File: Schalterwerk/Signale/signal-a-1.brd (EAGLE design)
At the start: 86 x 30.5 mm, 29 parts, among them Q1 NPN-23, Q2 NPN-23, Q3 NPN-23, Q4 NPN-23, X1 PHNX_4P_508CONN_1017493, X2 PHNX_4P_508CONN_1017493, X3 PHNX_4P_350CONN_1984989_PXC, X4 PHNX_4P_350CONN_1984989_PXC, X5 RJ45-JACK

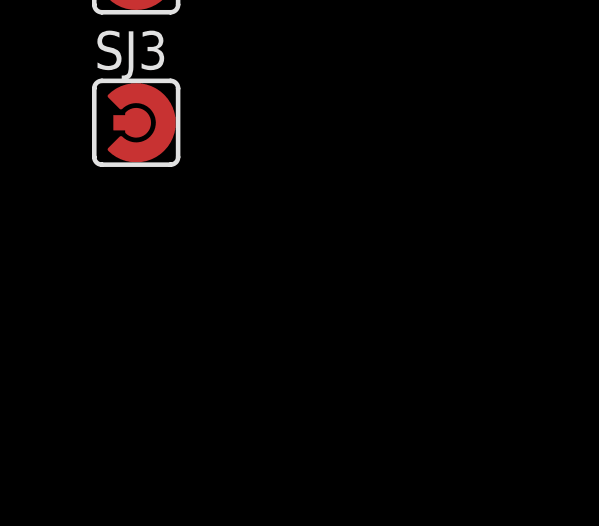
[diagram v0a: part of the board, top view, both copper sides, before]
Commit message: Adds LED.
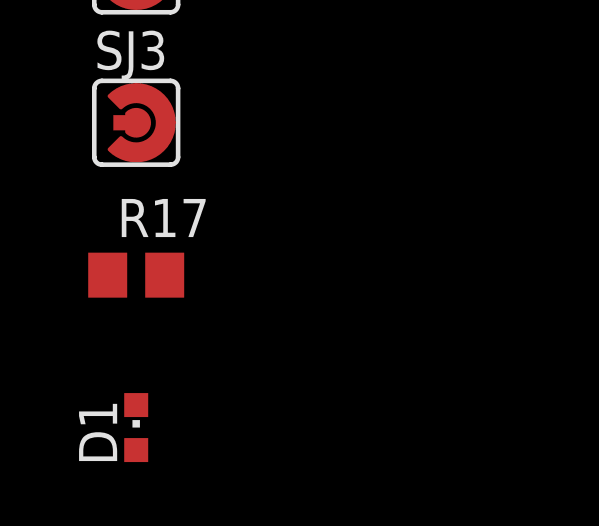
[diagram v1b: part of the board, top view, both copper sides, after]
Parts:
- added D1: (no value), led:CHIPLED_0603
- added R17: 1k5, rcl:R0805
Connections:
- new net GND1: D1.C
- new net N$24: R17.2
- new net N$25: D1.A, R17.1
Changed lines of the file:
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@@
 <attribute name="NAME" x="1.143" y="-362.712" size="1.27" layer="25" ratio="10"/>
+</element>
+<element name="D1" library="led" library_urn="urn:adsk.eagle:library:259" package="CHIPLED_0603" package3d_urn="urn:adsk.eagle:package:15822/2" value="" x="2.54" y="-374.65" smashed="yes">
+<attribute name="NAME" x="1.905" y="-375.92" size="1.27" layer="25" rot="R90"/>
+<attribute name="POPULARITY" value="28" x="-2.54" y="-363.22" size="1.778" layer="27" display="off"/>
+<attribute name="VALUE" x="4.445" y="-375.92" size="1.27" layer="27" rot="R90"/>
+</element>
+<element name="R17" library="rcl" library_urn="urn:adsk.eagle:library:334" package="R0805" package3d_urn="urn:adsk.eagle:package:23553/2" value="1k5" x="2.54" y="-369.57" smashed="yes">
+<attribute name="NAME" x="1.905" y="-368.3" size="1.27" layer="25"/>
+<attribute name="POPULARITY" value="86" x="-2.54" y="-369.57" size="1.778" layer="27" display="off"/>
+<attribute name="SPICEPREFIX" value="R" x="-2.54" y="-369.57" size="1.778" layer="27" display="off"/>
+<attribute name="VALUE" x="1.905" y="-372.11" size="1.27" layer="27"/>
 </element>
 </elements>
@@
 <wire x1="3.49" y1="-346.71" x2="19.05" y2="-199.39" width="0" layer="19" extent="1-1"/>
 </signal>
+<signal name="N$24">
+<contactref element="R17" pad="2"/>
+</signal>
+<signal name="GND1">
+<contactref element="D1" pad="C"/>
+</signal>
+<signal name="N$25">
+<contactref element="R17" pad="1"/>
+<contactref element="D1" pad="A"/>
+<wire x1="1.59" y1="-369.57" x2="2.54" y2="-375.4" width="0" layer="19" extent="1-1"/>
+</signal>
 </signals>
